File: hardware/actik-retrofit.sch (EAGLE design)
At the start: 45 parts, among them U1 TMP102, U5 2450AT18D0100-L, U6 MAX17048, U7 MIC5301, U8 NRF52832, Y4 32.768kHz

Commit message: hw: actik-retrofit: sent to fab, r0
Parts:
- added TP6: TPTP10R, testpad:TPTP10R
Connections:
- new net IO4: TP6.TP, U8.P0.29/AIN5
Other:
- moved on the sheet: C1, C16, C2, LED2, R1, R15, R2, R3, R4, R5, R6, R7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

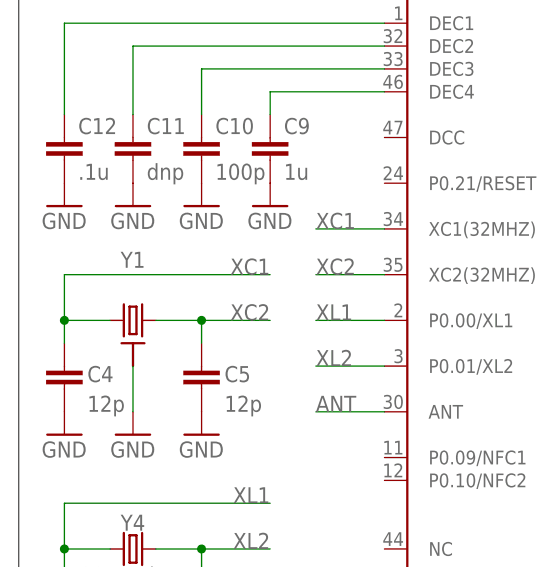
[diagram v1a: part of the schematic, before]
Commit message: hw: actik-retrofit: add xtal missing value
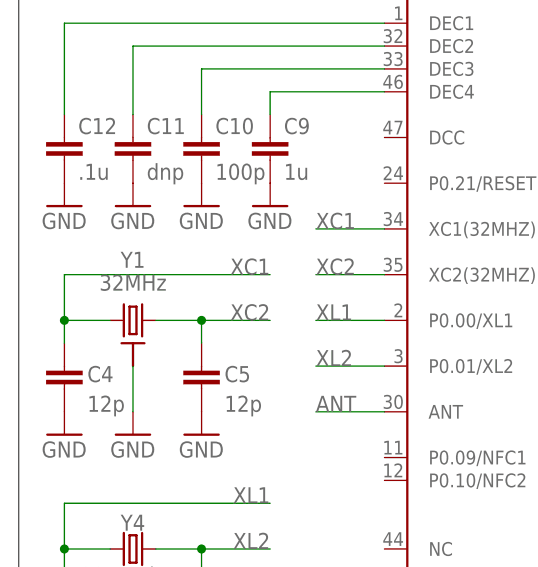
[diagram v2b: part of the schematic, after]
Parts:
- Y1: value (none) -> 32MHz
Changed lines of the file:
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@@
 <part name="U5" library="balto" deviceset="2450AT18D0100" device="-L" value="2450AT18D0100-L"/>
 <part name="GND22" library="supply1" deviceset="GND" device=""/>
-<part name="Y1" library="balto" deviceset="XTAL-GND" device="-2X1.6"/>
+<part name="Y1" library="balto" deviceset="XTAL-GND" device="-2X1.6" value="32MHz"/>
 <part name="GND35" library="supply1" deviceset="GND" device=""/>
 <part name="U1" library="balto" deviceset="TMP102" device=""/>
